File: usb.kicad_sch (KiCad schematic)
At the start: 4 parts, among them J9 USB_C_Receptacle_USB2.0_16P

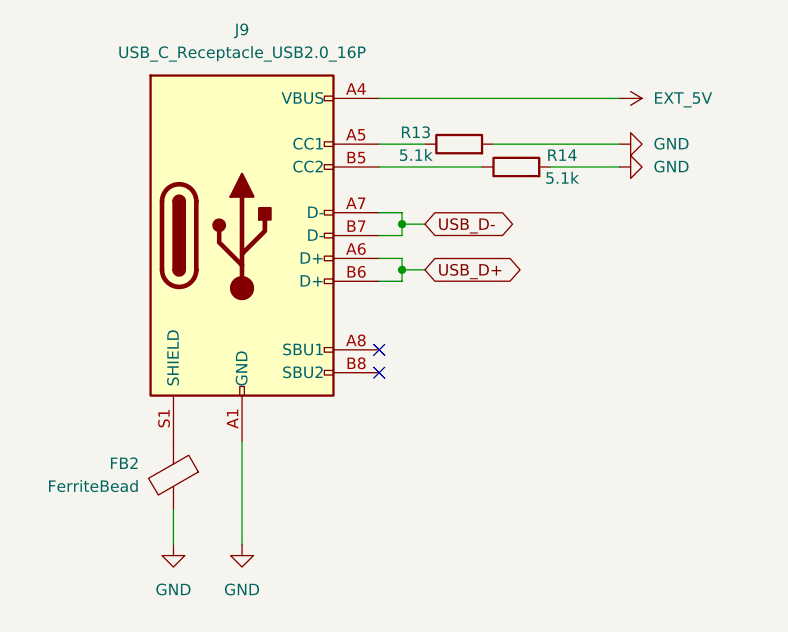
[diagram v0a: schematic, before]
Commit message: Added pin headers for SPI3, I2C0 and I2C1
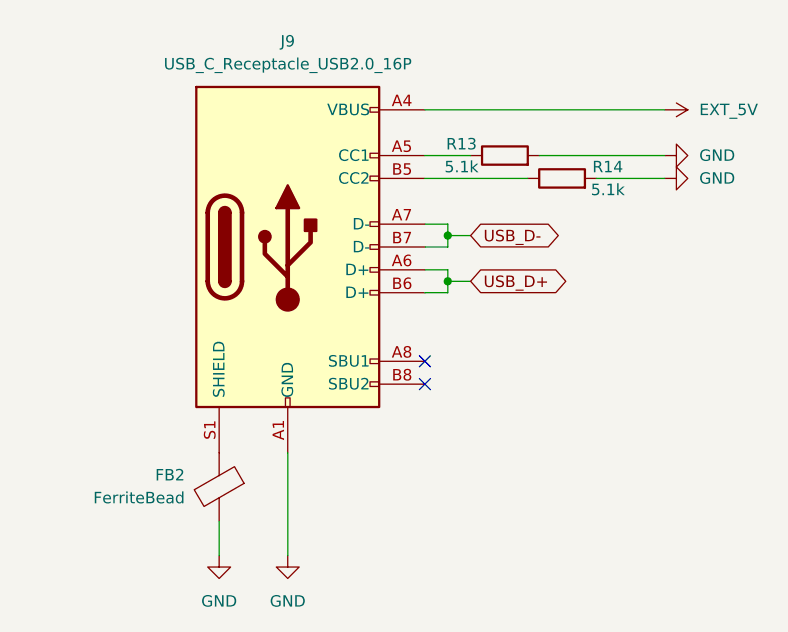
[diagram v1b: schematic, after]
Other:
- moved on the sheet: FB2, J9, R13, R14

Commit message: Correcting ERC errors
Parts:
- J9: symbol Connector:USB_C_Receptacle_USB2.0_16P -> noaidi-fpga-synth:USB_C_Receptacle_USB2.0_16P
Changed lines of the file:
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@@
 	)
 	(symbol
-		(lib_id "Connector:USB_C_Receptacle_USB2.0_16P")
+		(lib_id "noaidi-fpga-synth:USB_C_Receptacle_USB2.0_16P")
 		(at 137.16 99.06 0)
 		(unit 1)
@@
 		(pin "B5"
 		)
-		(pin "S4"
+		(pin "S1"
 		)
 		(pin "B6"
@@
 		(pin "S3"
 		)
-		(pin "S1"
+		(pin "S4"
 		)
 		(instances

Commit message: Added jumpers for FM and FIL to DAC. Added pin headers for audio out to DAC. Minor adjustments.
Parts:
- FB2: footprint (none) -> Inductor_SMD:L_0805_2012Metric_Pad1.05x1.20mm_HandSolder
- R13, R14: footprint (none) -> Resistor_THT:R_Axial_DIN0207_L6.3mm_D2.5mm_P10.16mm_Horizontal
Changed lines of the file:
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@@
+		(color 0 0 0 0)
+	)
+	(junction
+		(at 137.16 125.73)
+		(diameter 0)
 		(color 0 0 0 0)
 	)
@@
 	(wire
 		(pts
+			(xy 137.16 125.73) (xy 137.16 133.35)
+		)
+		(stroke
+			(width 0)
+			(type default)
+		)
+	)
+	(wire
+		(pts
 			(xy 154.94 97.79) (xy 157.48 97.79)
 		)
@@
 	(wire
 		(pts
+			(xy 137.16 121.92) (xy 137.16 125.73)
+		)
+		(stroke
+			(width 0)
+			(type default)
+		)
+	)
+	(wire
+		(pts
 			(xy 154.94 102.87) (xy 154.94 104.14)
 		)
@@
 		(pts
 			(xy 152.4 91.44) (xy 163.83 91.44)
-		)
-		(stroke
-			(width 0)
-			(type default)
-		)
-	)
-	(wire
-		(pts
-			(xy 137.16 121.92) (xy 137.16 133.35)
 		)
 		(stroke
@@
 			)
 		)
-		(property "Footprint" ""
+		(property "Footprint" "Inductor_SMD:L_0805_2012Metric_Pad1.05x1.20mm_HandSolder"
 			(at 131.318 125.73 90)
 			(hide yes)
@@
 			)
 		)
-		(property "Footprint" ""
+		(property "Footprint" "Resistor_THT:R_Axial_DIN0207_L6.3mm_D2.5mm_P10.16mm_Horizontal"
 			(at 167.64 93.218 90)
 			(hide yes)
@@
 			)
 		)
-		(property "Footprint" ""
+		(property "Footprint" "Resistor_THT:R_Axial_DIN0207_L6.3mm_D2.5mm_P10.16mm_Horizontal"
 			(at 161.29 90.678 90)
 			(hide yes)
@@
 					(unit 1)
 				)
+			)
+		)
+	)
+	(symbol
+		(lib_id "power:PWR_FLAG")
+		(at 137.16 125.73 270)
+		(unit 1)
+		(body_style 1)
+		(exclude_from_sim no)
+		(in_bom yes)
+		(on_board yes)
+		(in_pos_files yes)
+		(dnp no)
+		(fields_autoplaced yes)
+		(property "Reference" "#FLG01"
+			(at 139.065 125.73 0)
+			(hide yes)
+			(show_name no)
+			(do_not_autoplace no)
+			(effects
+				(font
+					(size 1.27 1.27)
+				)
+			)
+		)
+		(property "Value" "PWR_FLAG"
+			(at 140.97 125.7299 90)
+			(show_name no)
+			(do_not_autoplace no)
+			(effects
+				(font
+					(size 1.27 1.27)
+				)
+				(justify left)
+			)
+		)
+		(property "Footprint" "Package_DIP:DIP-24_W7.62mm"
+			(at 137.16 125.73 0)
+			(hide yes)
+			(show_name no)
+			(do_not_autoplace no)
+			(effects
+				(font
+					(size 1.27 1.27)
+				)
+			)
+		)
+		(property "Datasheet" ""
+			(at 137.16 125.73 0)
+			(hide yes)
+			(show_name no)
+			(do_not_autoplace no)
+			(effects
+				(font
+					(size 1.27 1.27)
+				)
+			)
+		)
+		(property "Description" "Special symbol for telling ERC where power comes from"
+			(at 137.16 125.73 0)
+			(hide yes)
+			(show_name no)
+			(do_not_autoplace no)
+			(effects
+				(font
+					(size 1.27 1.27)
+				)
+			)
+		)
+		(pin "1"
+		)
+		(instances
+			(project "noaidi-fpga-synth"
+				(path "/ac0f489c-9b9e-476a-83a1-244c132c2581"
+					(reference "#FLG01")
+					(unit 1)
+				)
